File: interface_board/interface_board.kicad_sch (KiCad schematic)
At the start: 6 parts, among them J1 FPGA_devboard, J2 5V_PWR

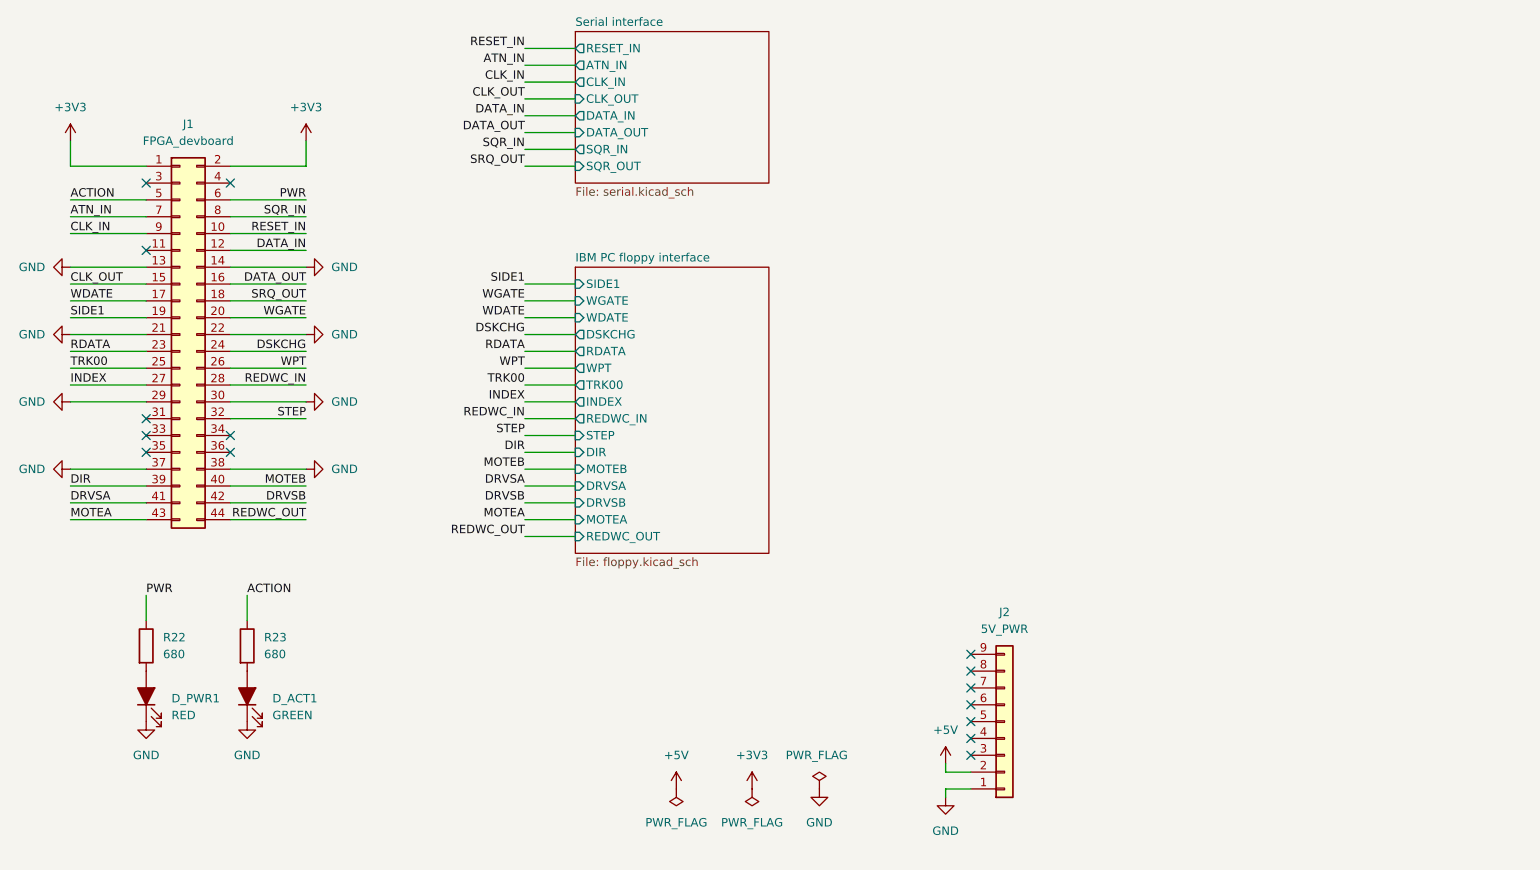
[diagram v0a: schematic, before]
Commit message: Add schematics for appendix, add sketch to diploma, simulate startup in isim
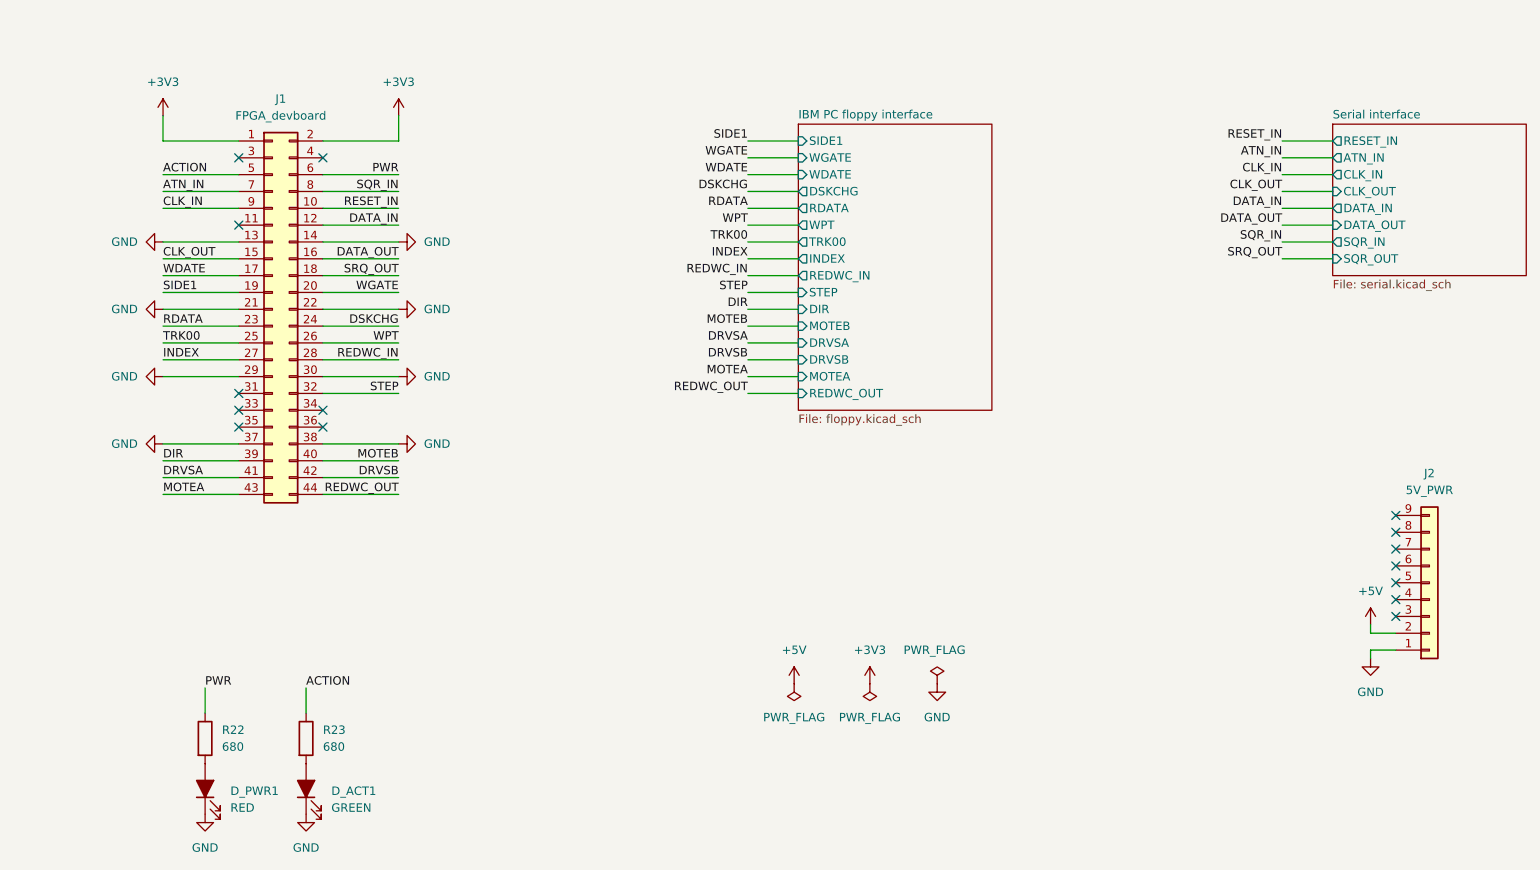
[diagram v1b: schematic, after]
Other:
- moved on the sheet: D_ACT1, D_PWR1, J1, J2, R22, R23
